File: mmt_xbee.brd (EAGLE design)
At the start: 204.4 x 88.6 mm, 134 parts, among them IC1 P82B715D, J1 6473427-1, J2 VR10S05, Q1 MOSFET-NCHANNELSMD, Q2 MOSFET-NCHANNELSMD, SW1 CTS_ELECTROCOMPONENTS_204-211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, SW2 CTS_ELECTROCOMPONENTS_204-211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, U1 XC6220B331MR-G, U4 ARDUINO_R3_SHIELD, U6 ADS1119IPWT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

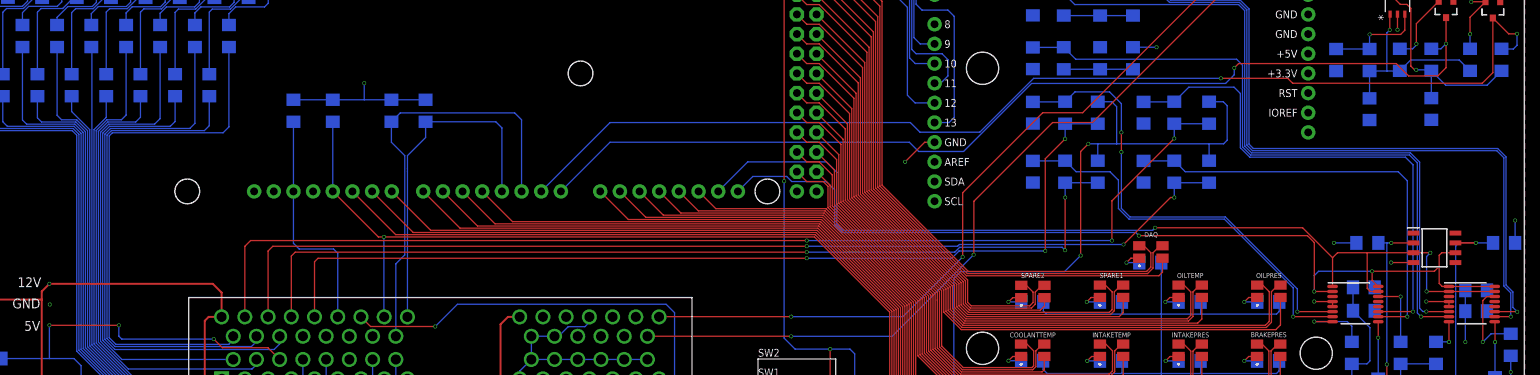
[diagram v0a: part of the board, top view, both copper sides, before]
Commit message: Fixed keepout on XBee and modified testing vias
Removed all the copper (top & bottom) at the top of the XBee
Made testing vias bigger
Added a 3.3V testing via
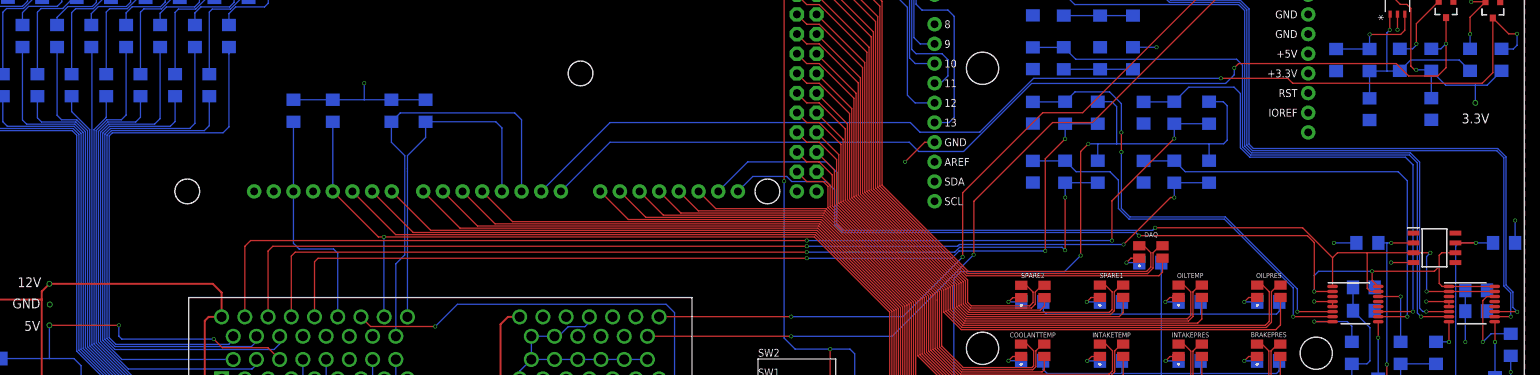
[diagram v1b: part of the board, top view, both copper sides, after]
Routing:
- net 3.3V: track 45.2 -> 47.5 mm, vias 2 -> 3
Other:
- board text added: "3.3V"
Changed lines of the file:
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@@
 <layer number="37" name="tTest" color="7" fill="1" visible="no" active="yes"/>
 <layer number="38" name="bTest" color="7" fill="1" visible="no" active="yes"/>
-<layer number="39" name="tKeepout" color="4" fill="11" visible="no" active="yes"/>
-<layer number="40" name="bKeepout" color="1" fill="11" visible="no" active="yes"/>
-<layer number="41" name="tRestrict" color="4" fill="10" visible="no" active="yes"/>
-<layer number="42" name="bRestrict" color="1" fill="10" visible="no" active="yes"/>
-<layer number="43" name="vRestrict" color="2" fill="10" visible="no" active="yes"/>
+<layer number="39" name="tKeepout" color="4" fill="11" visible="yes" active="yes"/>
+<layer number="40" name="bKeepout" color="1" fill="11" visible="yes" active="yes"/>
+<layer number="41" name="tRestrict" color="4" fill="10" visible="yes" active="yes"/>
+<layer number="42" name="bRestrict" color="1" fill="10" visible="yes" active="yes"/>
+<layer number="43" name="vRestrict" color="2" fill="10" visible="yes" active="yes"/>
 <layer number="44" name="Drills" color="7" fill="1" visible="yes" active="yes"/>
 <layer number="45" name="Holes" color="7" fill="1" visible="yes" active="yes"/>
@@
 </layers>
 <board>
-<fusionsync huburn="a.YnVzaW5lc3M6bXl1MzQyNjY" projecturn="a.YnVzaW5lc3M6bXl1MzQyNjYjRDIwMjIwMjIzNTAwNDUzMjU2" f3durn="urn:adsk.wipprod:dm.lineage:r1dzTaXARS2bTS1gvLIk1Q" pcbguid="" lastpulledtime="" lastsyncedchangeguid="" latestrevisionid="da83cb01-ae74-4442-8c85-13959e2adcd9" lastsyncedrevisionid="da83cb01-ae74-4442-8c85-13959e2adcd9" lastboardhashguid="5f2a0044-59c8-55ce-d47b-bb62881ef927" lastpushedtime="2022-03-29T21:23:44Z" linktopcb3d="true"/>
+<fusionsync huburn="a.YnVzaW5lc3M6bXl1MzQyNjY" projecturn="a.YnVzaW5lc3M6bXl1MzQyNjYjRDIwMjIwMjIzNTAwNDUzMjU2" f3durn="urn:adsk.wipprod:dm.lineage:r1dzTaXARS2bTS1gvLIk1Q" pcbguid="" lastpulledtime="" lastsyncedchangeguid="" latestrevisionid="2d7ccddb-5392-461c-a377-a269c7bc2a62" lastsyncedrevisionid="2d7ccddb-5392-461c-a377-a269c7bc2a62" lastboardhashguid="2732d0dc-69c0-ad12-dcd4-0261fa5c63f2" lastpushedtime="2022-03-30T00:19:29Z" linktopcb3d="true"/>
 <plain>
 <wire x1="-13.97" y1="53.34" x2="190.48" y2="53.34" width="0" layer="20"/>
@@
 <text x="-3.2766" y="69.6214" size="1.27" layer="21">5V</text>
 <text x="-4.8006" y="72.517" size="1.27" layer="21">GND</text>
+<polygon width="0.1524" layer="41">
+<vertex x="184.15" y="130.4798"/>
+<vertex x="190.9826" y="130.4798"/>
+<vertex x="190.9826" y="118.8974"/>
+<vertex x="184.15" y="118.8974"/>
+</polygon>
+<polygon width="0.1524" layer="42">
+<vertex x="184.15" y="130.4798"/>
+<vertex x="190.9826" y="130.4798"/>
+<vertex x="190.9826" y="118.8974"/>
+<vertex x="184.15" y="118.8974"/>
+</polygon>
+<text x="182.3974" y="96.4184" size="1.27" layer="21">3.3V</text>
 </plain>
 <attributes>
@@
 <attribute name="MOUSER_PRICE-STOCK" value="https://www.mouser.co.uk/ProductDetail/Texas-Instruments/P82B715D?qs=ToK3%2FczOkx%2Fmhyx%252Bp5%2FQZw%3D%3D" x="178.8668" y="80.3402" size="1.778" layer="27" display="off"/>
 </element>
-<element name="U1" library="XC6220B331MR-G" package="SOT-25_TOR" override_package3d_urn="urn:adsk.eagle:package:34557894/2" override_package_urn="urn:adsk.eagle:footprint:34557895/1" value="XC6220B331MR-G" x="174.0916" y="111.8108" smashed="yes" rot="R90">
+<element name="U1" library="XC6220B331MR-G" package="SOT-25_TOR" override_package3d_urn="urn:adsk.eagle:package:34557894/2" override_package_urn="urn:adsk.eagle:footprint:34557895/1" override_locally_modified="yes" value="XC6220B331MR-G" x="174.0916" y="111.8108" smashed="yes" rot="R90">
 <attribute name="COPYRIGHT" value="Copyright (C) 2022 Ultra Librarian. All rights reserved." x="174.0916" y="111.8108" size="1.778" layer="27" rot="R90" display="off"/>
 <attribute name="DIGI-KEY_PART_NUMBER_1" value="893-1133-1-ND" x="174.0916" y="111.8108" size="1.778" layer="27" rot="R90" display="off"/>
@@
 <attribute name="MFR_NAME" value="Torex Semiconductor" x="174.0916" y="111.8108" size="1.778" layer="27" rot="R90" display="off"/>
 </element>
-<element name="J2" library="VR10S05" package="CONN3_10S05_XPP" override_package3d_urn="urn:adsk.eagle:package:34567845/2" override_package_urn="urn:adsk.eagle:footprint:34567846/1" value="VR10S05" x="-1.016" y="60.8076" smashed="yes">
+<element name="J2" library="VR10S05" package="CONN3_10S05_XPP" override_package3d_urn="urn:adsk.eagle:package:34567845/2" override_package_urn="urn:adsk.eagle:footprint:34567846/1" override_locally_modified="yes" value="VR10S05" x="-1.016" y="60.8076" smashed="yes">
 <attribute name="COPYRIGHT" value="Copyright (C) 2022 Ultra Librarian. All rights reserved." x="-1.016" y="60.8076" size="1.778" layer="27" display="off"/>
 <attribute name="DIGI-KEY_PART_NUMBER_1" value="1470-VR10S05-ND" x="-1.016" y="60.8076" size="1.778" layer="27" display="off"/>
@@
 <contactref element="J1" pad="26"/>
 <contactref element="J1" pad="54"/>
-<via x="-0.0254" y="75.692" extent="1-16" drill="0.35"/>
+<via x="-0.0254" y="75.692" extent="1-16" drill="0.508"/>
 <contactref element="J2" pad="1"/>
 <wire x1="-1.016" y1="73.66" x2="-1.016" y2="74.7014" width="0.254" layer="1"/>
@@
 <contactref element="IC1" pad="8"/>
 <contactref element="U1" pad="1"/>
-<via x="-0.0254" y="70.3326" extent="1-16" drill="0.35"/>
+<via x="-0.0254" y="70.3326" extent="1-16" drill="0.508"/>
 <contactref element="J2" pad="3"/>
 <contactref element="R1" pad="2"/>
@@
 <wire x1="178.4604" y1="103.2006" x2="180.315" y2="101.346" width="0.1524" layer="16"/>
 <wire x1="185.6736" y1="101.346" x2="187.5282" y2="103.2006" width="0.1524" layer="16"/>
-<wire x1="180.315" y1="101.346" x2="185.6736" y2="101.346" width="0.1524" layer="16"/>
+<wire x1="180.315" y1="101.346" x2="184.15" y2="101.346" width="0.1524" layer="16"/>
+<wire x1="184.15" y1="101.346" x2="185.6736" y2="101.346" width="0.1524" layer="16"/>
 <wire x1="173.1416" y1="113.09985" x2="174.45605" y2="111.7854" width="0.1524" layer="1"/>
 <wire x1="175.8188" y1="111.2774" x2="175.8188" y2="103.8098" width="0.1524" layer="1"/>
@@
 <wire x1="174.45605" y1="111.7854" x2="175.3108" y2="111.7854" width="0.1524" layer="1"/>
 <wire x1="175.3108" y1="111.7854" x2="175.8188" y2="111.2774" width="0.1524" layer="1"/>
+<wire x1="184.15" y1="101.346" x2="184.15" y2="99.06" width="0.1524" layer="16"/>
+<via x="184.15" y="99.06" extent="1-16" drill="0.508"/>
 </signal>
 <signal name="SD_CS">
@@
 <contactref element="J1" pad="18"/>
 <contactref element="R25" pad="1"/>
-<wire x1="23.1648" y1="95.9612" x2="23.1648" y2="106.274" width="0.1524" layer="16"/>
+<wire x1="23.1648" y1="95.9612" x2="23.1648" y2="105.41" width="0.1524" layer="16"/>
+<wire x1="23.1648" y1="105.41" x2="23.1648" y2="106.274" width="0.1524" layer="16"/>
 <wire x1="7.6962" y1="94.7954375" x2="8.0999625" y2="95.1992" width="0.1524" layer="16"/>
 <wire x1="8.0999625" y1="95.1992" x2="22.4028" y2="95.1992" width="0.1524" layer="16"/>
@@
 </signal>
 <signal name="N$3">
-<via x="0.0254" y="73.025" extent="1-16" drill="0.35"/>
+<via x="0.0254" y="73.025" extent="1-16" drill="0.508"/>
 </signal>
 <signal name="N$4">
